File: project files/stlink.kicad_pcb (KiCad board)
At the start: 2 copper layers, 43.2 x 17.8 mm, 63 parts, among them J1 USB Type C, J2 Power Target, J3 Self, J4 STDC-14, J5 Target, Q1 MMBT9013, U1 STM32F103CBTx, U2 STM32F103CBUx, U3 AMS1117-3.3, Y1 8MHz

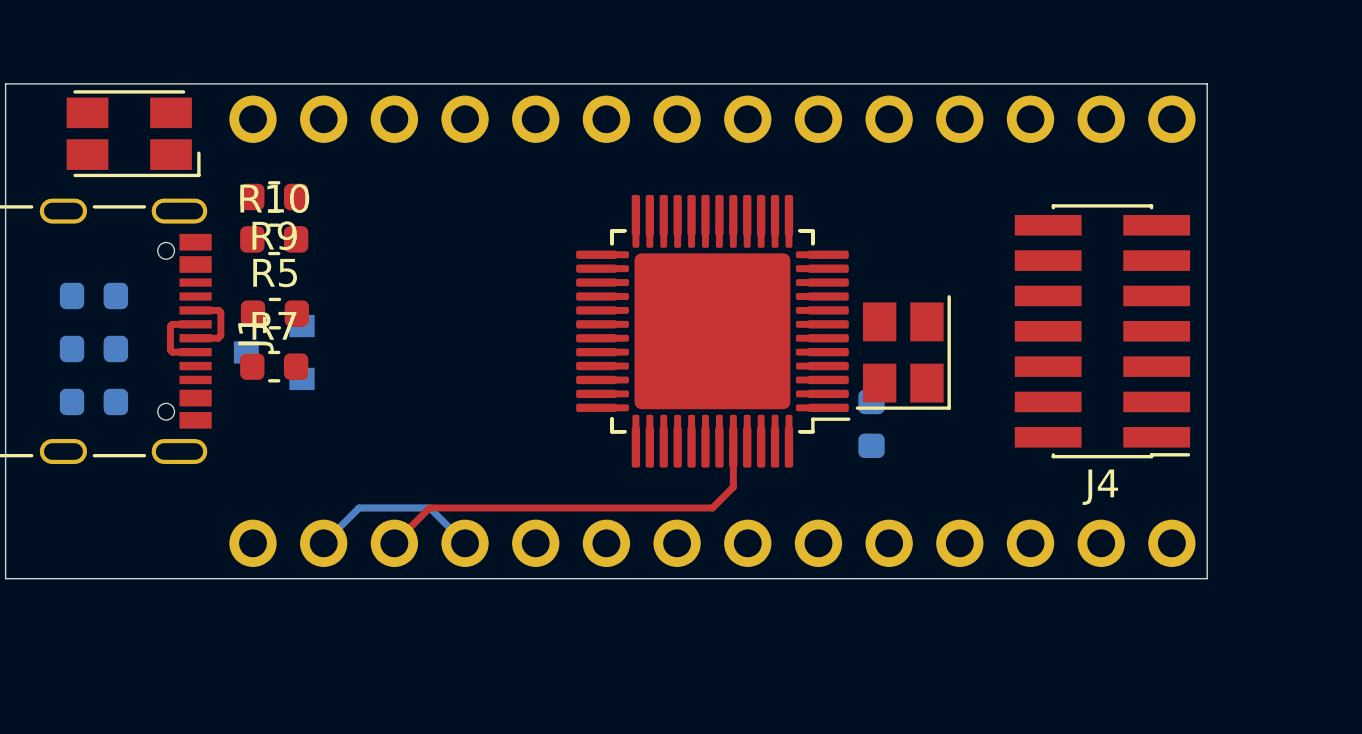
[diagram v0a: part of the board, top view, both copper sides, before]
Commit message: multi-sheet introduction for spare parts
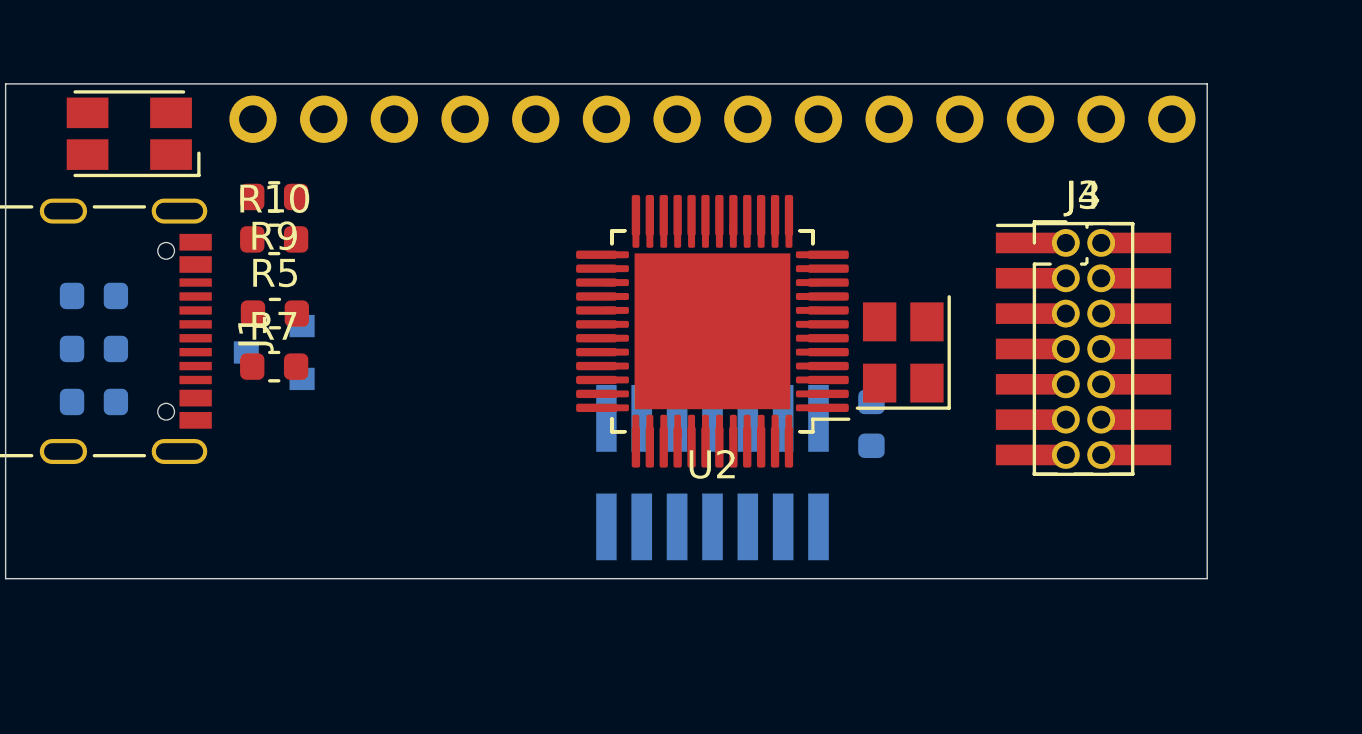
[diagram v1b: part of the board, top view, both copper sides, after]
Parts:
- added J6: Self, Connector_PinHeader_1.27mm:PinHeader_2x07_P1.27mm_Vertical_SMD, B.Cu at (232.4, 121.9)
- J3: value Self -> Target STDC-14; footprint Connector_PinHeader_2.54mm:PinHeader_1x14_P2.54mm_Vertical -> Connector_PinHeader_1.27mm:PinHeader_2x07_P1.27mm_Vertical_SMD; moved to F.Cu
- J4: value STDC-14 -> Target STDC-14; footprint Connector_PinHeader_1.27mm:PinHeader_2x07_P1.27mm_Vertical_SMD -> Connector_PinHeader_1.27mm:PinHeader_2x07_P1.27mm_Vertical
- moved J3 30.7 mm to (245.7, 117.5), turned to 0 degrees
- moved J4 3.44 mm to (245.1, 113.7), turned to 0 degrees
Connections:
- J3 pad 1: +5V -> (no net)
- J3 pad 10: Self_SWDCLK(h) -> T_JTDI(h)
- J3 pad 12: Self_SWDIO(h) -> T_NRST_SWD(h)
- J3 pad 13: Self_NRST(h) -> T_VCP_RX(h)
- J3 pad 14: Self_SWO(h) -> T_VCP_TX(h)
- J3 pad 2: +3V3 -> (no net)
- J3 pad 3: BOOT_0(h) -> T_Vref
- J3 pad 4: +3V3 -> T_SWDIO(h)
- J3 pad 5: Self_TX(h) -> GND_detect(h)
- J3 pad 6: Self_RX(h) -> T_SWDCLK(h)
- J3 pad 8: (no net) -> T_SWO(h)
- J3 pad 9: +3V3 -> (no net)
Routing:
- net BOOT_0(h): track 14.5 -> 0.00 mm
- net +3V3: track 6.13 -> 0.00 mm
- net /D+: track 2.72 -> 0.00 mm
- net /D-: track 2.71 -> 0.00 mm

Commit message: some rerouting
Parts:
- removed the U2 at (232.4, 116.8)
- added U3: STM32F103CBUx, Package_DFN_QFN:QFN-48-1EP_7x7mm_P0.5mm_EP5.6x5.6mm, F.Cu at (232.4, 116.8)
- renumbered C8 to C10, C14 to C11, C11 to C13, C15 to C14, C9 to C15, C10 to C8, C13 to C9, D4 to D3, D3 to D4, J5 to J2, J2 to J3, J6 to J4, J4 to J5, J3 to J6, R13 to R10, R12 to R11, R16 to R12, R14 to R13, R15 to R14, R18 to R15, R17 to R16, R19 to R17, R20 to R18, R21 to R19, R22 to R20, R23 to R21, R24 to R22, R25 to R23, R26 to R24, R27 to R25, R28 to R26, R29 to R27, R30 to R28, R31 to R29, R32 to R30, R33 to R31, R34 to R32, R5 to R4, R6 to R5, R7 to R6, R9 to R7, R10 to R8, R11 to R9, U3 to U2
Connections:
- net /AIN renamed AIN
- net /Board_ID renamed Board_ID
- net /STLINK_OSC_IN renamed OSC_IN
- net /STLINK_OST_OUT renamed OSC_OUT
- net /STLINK_RX renamed STLINK_RX
- net /STLINK_TX renamed STLINK_TX
- net /STLINK_USB_D+ renamed STLINK_USB_D+
- net /STLINK_USB_D- renamed STLINK_USB_D-
- net /T_JTDI renamed T_JTDI
- net /T_NRST_SWD renamed T_NRST_SWD
- net /T_NRST_SWIM renamed T_NRST_SWIM
- net /T_NRST_SWIM_IN renamed T_NRST_SWIM_IN
- net /T_SWDCLK renamed T_SWDCLK
- net /T_SWDIO renamed T_SWDIO
- net /T_SWDIO_IN renamed T_SWDIO_IN
- net /T_SWIM renamed T_SWIM
- net /T_SWIM_IN renamed T_SWIM_IN
- net /USB_RENUMn renamed USB_RENUMn
- net BOOT_0(h) renamed BOOT_0
- net GND_detect(h) renamed BOOT_1
- net Self_NRST(h) renamed SELF_NRST
- net Self_SWDCLK(h) renamed SWDCLK
- net Self_SWDIO(h) renamed SWDIO
- net Self_SWO(h) renamed SWO
- J4 pad 14: Self_TX(h) -> STLINK_LED
- R10 pad 2: Self_TX(h) -> (no net)
- R11 pad 2: Self_TX(h) -> STLINK_LED
- U1 pad 30: Self_TX(h) -> STLINK_LED
